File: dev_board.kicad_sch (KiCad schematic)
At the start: 41 parts, among them J1 USB_C_Receptacle_USB2.0_16P, J2 Conn_01x20_Pin, J3 Conn_01x20_Pin, J4 Conn_01x04_Pin, SW1 SW_SPST, SW2 SW_SPST, U1 STM32F103C8Tx, U2 AMS1117-3.3, U3 USBLC6-2SC6, Y1 16MHz

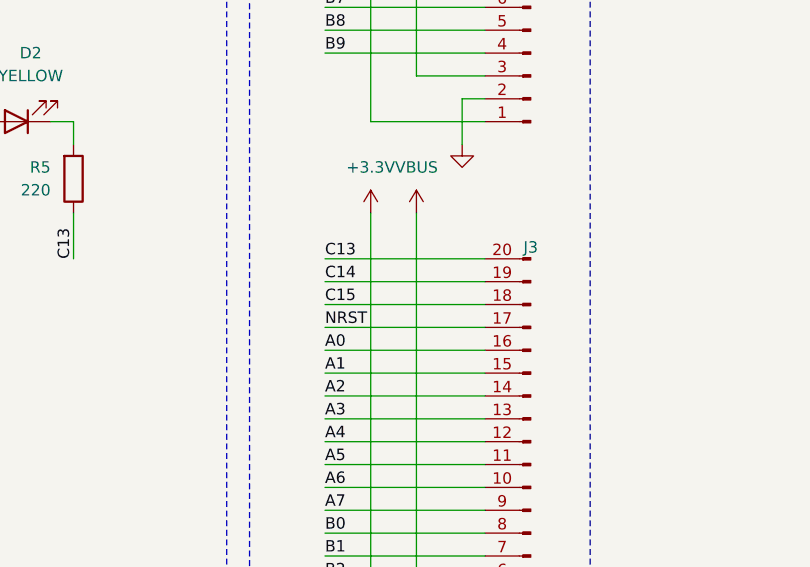
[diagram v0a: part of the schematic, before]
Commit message: opt: zone fills and remove some vias after feedback
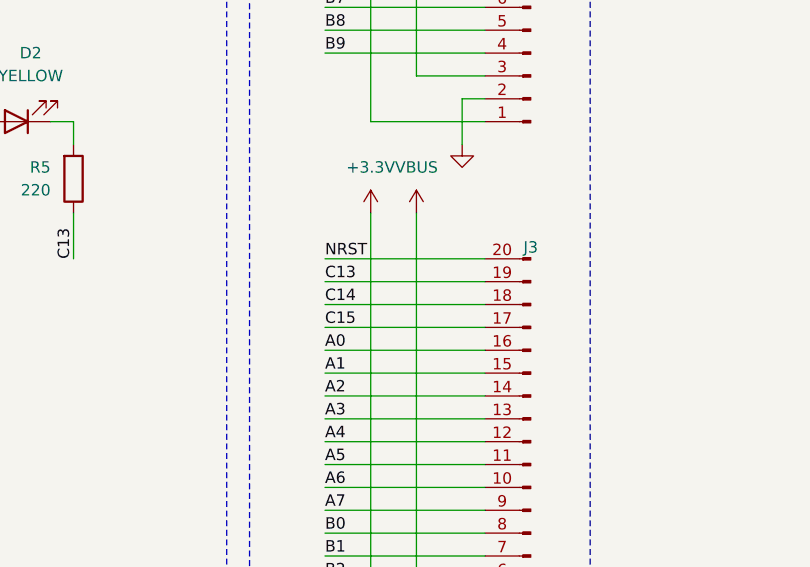
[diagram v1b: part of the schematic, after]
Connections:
- net C13: now also J3.19 (Pin_19); no longer J3.20 (Pin_20)
- net C14: now also J3.18 (Pin_18); no longer J3.19 (Pin_19)
- net C15: now also J3.17 (Pin_17); no longer J3.18 (Pin_18)
- net NRST: now also J3.20 (Pin_20); no longer J3.17 (Pin_17)
